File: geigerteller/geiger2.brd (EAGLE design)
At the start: 100 x 60 mm, 56 parts, among them J1 AVR_SPI_PRG_6PTH, Q1 NFET, Q2 MMBT5088, Q4 MMBT5088, Q5 MMBT5088, U1 ATMEGA328P, U2 MAX1555, U3 LCD-16X2SILK, U4 FT232RL-BASICSSOP, U5 MC34063SMD

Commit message: Moved drill holes and Q5
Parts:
- moved Q5 6.56 mm to (5.75, 53.2), turned to 270 degrees
- moved R1 5.06 mm to (2.50, 50.2)
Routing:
- net N$5: track 149.1 -> 135.2 mm
- net RESET: track 92.7 -> 82.5 mm
- net N$2: track 48.9 -> 54.1 mm
- net N$24: track 12.7 -> 9.82 mm
- net 12V: track 129.4 -> 127.6 mm
- net N$4: track 3.37 -> 4.73 mm
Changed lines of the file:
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@@
 <wire x1="100" y1="60" x2="0" y2="60" width="0" layer="20"/>
 <wire x1="0" y1="60" x2="0" y2="0" width="0" layer="20"/>
-<hole x="5.65" y="54.45" drill="3.2"/>
-<hole x="94.5" y="54.5" drill="3.2"/>
-<hole x="5.5" y="5.5" drill="3.2"/>
-<wire x1="0.25" y1="38.25" x2="99.5" y2="38.25" width="1.016" layer="51" style="longdash"/>
-<hole x="95.25" y="3.5" drill="3.2"/>
+<hole x="3" y="57" drill="3.2"/>
+<hole x="97" y="57" drill="3.2"/>
+<hole x="3" y="3" drill="3.2"/>
+<wire x1="0.25" y1="38.25" x2="99.5" y2="38.25" width="1.016" layer="121" style="longdash"/>
+<hole x="97" y="3" drill="3.2"/>
 </plain>
 <attributes>
@@
 <attribute name="NAME" x="74.891" y="54.202" size="0.4064" layer="25"/>
 </element>
-<element name="R1" library="rcl" package="R0603" value="330" x="7.25" y="48.5" smashed="yes" rot="R90">
-<attribute name="NAME" x="5.615" y="47.115" size="1.27" layer="25" rot="R90"/>
+<element name="R1" library="rcl" package="R0603" value="330" x="2.5" y="50.25" smashed="yes" rot="R90">
+<attribute name="NAME" x="4.615" y="49.615" size="1.27" layer="25" rot="R90"/>
 </element>
 <element name="R2" library="rcl" package="0207/10" value="" x="54.5" y="55.25" smashed="yes">
@@
 </element>
 <element name="U$2" library="henriks_egne_pakker" package="SOT23" value="XC6026" x="79.75" y="7.25" rot="R270"/>
-<element name="Q5" library="SparkFun-DiscreteSemi" package="SOT23" value="MMBT5088" x="10.75" y="49">
-<attribute name="PROD_ID" value="TRANS-11160" x="10.75" y="49" size="1.778" layer="27" display="off"/>
+<element name="Q5" library="SparkFun-DiscreteSemi" package="SOT23" value="MMBT5088" x="5.75" y="53.25" smashed="yes" rot="R270">
+<attribute name="PROD_ID" value="TRANS-11160" x="5.75" y="53.25" size="1.778" layer="27" rot="R270" display="off"/>
+<attribute name="NAME" x="5.611" y="50.532" size="1.016" layer="25"/>
 </element>
 <element name="R14" library="rcl" package="R0603" value="10k" x="8.7" y="56.7" smashed="yes" rot="R270">
@@
 <wire x1="35.25" y1="38.5" x2="33.25" y2="40.5" width="0.3048" layer="1"/>
 <wire x1="33.25" y1="40.5" x2="31.75" y2="40.5" width="0.3048" layer="1"/>
-<wire x1="7.25" y1="47.65" x2="7.25" y2="46.25" width="0.4064" layer="1"/>
 <via x="7.25" y="46.25" extent="1-16" drill="0.6" shape="octagon"/>
 <wire x1="7.25" y1="46.25" x2="7.25" y2="43.5" width="0.4064" layer="16"/>
 <wire x1="7.25" y1="43.5" x2="7.5" y2="43.25" width="0.4064" layer="16"/>
 <wire x1="7.5" y1="43.25" x2="10.75" y2="43.25" width="0.4064" layer="16"/>
+<wire x1="7.25" y1="46.25" x2="7.25" y2="47.25" width="0.4064" layer="1"/>
+<wire x1="7.25" y1="47.25" x2="5.5" y2="49" width="0.4064" layer="1"/>
+<wire x1="5.5" y1="49" x2="2.9" y2="49" width="0.4064" layer="1"/>
+<wire x1="2.9" y1="49" x2="2.5" y2="49.4" width="0.4064" layer="1"/>
 </signal>
 <signal name="N$3">
@@
 <wire x1="93.5" y1="37.5" x2="93.5" y2="29.5" width="0.3048" layer="16"/>
 <wire x1="93.5" y1="29.5" x2="95.25" y2="27.75" width="0.3048" layer="16"/>
-<wire x1="98.5" y1="6" x2="98.5" y2="1.5" width="0.3048" layer="1"/>
-<wire x1="91.5" y1="1.75" x2="91.5" y2="5.46" width="0.3048" layer="1"/>
-<wire x1="91.5" y1="5.46" x2="92.21" y2="5.46" width="0.3048" layer="1"/>
-<wire x1="92.21" y1="5.46" x2="93" y2="6.25" width="0.3048" layer="1"/>
-<wire x1="93" y1="6.25" x2="93" y2="7.46" width="0.3048" layer="1"/>
-<wire x1="93" y1="7.46" x2="93.54" y2="8" width="0.3048" layer="1"/>
 <wire x1="99" y1="6.5" x2="99" y2="9" width="0.3048" layer="16"/>
 <wire x1="99" y1="9" x2="98.5" y2="9.5" width="0.3048" layer="16"/>
@@
 <wire x1="95.5" y1="13" x2="95.25" y2="13.25" width="0.3048" layer="16"/>
 <wire x1="95.25" y1="13.25" x2="95.25" y2="27.75" width="0.3048" layer="16"/>
-<wire x1="98.5" y1="1.5" x2="97.75" y2="0.75" width="0.3048" layer="1"/>
-<wire x1="97.75" y1="0.75" x2="92.5" y2="0.75" width="0.3048" layer="1"/>
-<wire x1="92.5" y1="0.75" x2="91.5" y2="1.75" width="0.3048" layer="1"/>
+<wire x1="98.5" y1="6" x2="95.54" y2="6" width="0.3048" layer="1"/>
+<wire x1="95.54" y1="6" x2="93.54" y2="8" width="0.3048" layer="1"/>
 </signal>
 <signal name="N$6">
@@
 <via x="87.25" y="5.5" extent="1-16" drill="0.6" shape="octagon"/>
 <wire x1="87.25" y1="5.5" x2="90.25" y2="5.5" width="0.3048" layer="16"/>
-<wire x1="98.25" y1="4.75" x2="97.75" y2="5.25" width="0.3048" layer="16"/>
-<wire x1="97.75" y1="5.25" x2="97.75" y2="5.5" width="0.3048" layer="16"/>
-<wire x1="97.75" y1="5.5" x2="97.25" y2="6" width="0.3048" layer="16"/>
 <wire x1="97.25" y1="6" x2="97.25" y2="7.5" width="0.3048" layer="16"/>
 <wire x1="97.25" y1="7.5" x2="96.58" y2="7.5" width="0.3048" layer="16"/>
@@
 <wire x1="85.75" y1="5.75" x2="86" y2="5.5" width="0.3048" layer="16"/>
 <wire x1="86" y1="5.5" x2="87.25" y2="5.5" width="0.3048" layer="16"/>
-<wire x1="90.25" y1="5.5" x2="90.25" y2="2.25" width="0.3048" layer="16"/>
-<wire x1="90.25" y1="2.25" x2="91.75" y2="0.75" width="0.3048" layer="16"/>
-<wire x1="91.75" y1="0.75" x2="98" y2="0.75" width="0.3048" layer="16"/>
-<wire x1="98" y1="0.75" x2="98.25" y2="1" width="0.3048" layer="16"/>
-<wire x1="98.25" y1="1" x2="98.25" y2="4.75" width="0.3048" layer="16"/>
+<wire x1="97.25" y1="6" x2="97" y2="5.75" width="0.3048" layer="16"/>
+<wire x1="97" y1="5.75" x2="90.5" y2="5.75" width="0.3048" layer="16"/>
+<wire x1="90.5" y1="5.75" x2="90.25" y2="5.5" width="0.3048" layer="16"/>
 </signal>
 <signal name="LCD_E">
@@
 <wire x1="15" y1="52.25" x2="13.75" y2="51" width="0.3048" layer="1"/>
 <via x="13.75" y="51" extent="1-16" drill="0.6" shape="octagon"/>
-<wire x1="13.75" y1="51" x2="7.5" y2="51" width="0.3048" layer="16"/>
-<via x="7.5" y="51" extent="1-16" drill="0.6" shape="octagon"/>
-<wire x1="7.5" y1="51" x2="7.5" y2="53" width="0.3048" layer="1"/>
-<wire x1="7.5" y1="53" x2="8.75" y2="54.25" width="0.3048" layer="1"/>
-<wire x1="8.75" y1="54.25" x2="8.75" y2="55.8" width="0.3048" layer="1"/>
+<wire x1="13.75" y1="51" x2="8.75" y2="51" width="0.3048" layer="16"/>
+<via x="8.75" y="51" extent="1-16" drill="0.6" shape="octagon"/>
 <wire x1="8.75" y1="55.8" x2="8.7" y2="55.85" width="0.3048" layer="1"/>
 <via x="34" y="47.5" extent="1-16" drill="0.6" shape="octagon"/>
@@
 <wire x1="31.5" y1="57.25" x2="31.5" y2="55.1681" width="0.3048" layer="1"/>
 <wire x1="31.5" y1="55.1681" x2="31.4919" y2="55.16" width="0.3048" layer="1"/>
+<wire x1="8.75" y1="55.8" x2="8.75" y2="51" width="0.4064" layer="1"/>
 </signal>
 <signal name="N$4">
 <contactref element="R1" pad="2"/>
 <contactref element="Q5" pad="1"/>
-<wire x1="9.8" y1="47.9" x2="9.8" y2="48.2" width="0.4064" layer="1"/>
-<wire x1="9.8" y1="48.2" x2="8.6" y2="49.4" width="0.4064" layer="1"/>
-<wire x1="8.6" y1="49.4" x2="7.3" y2="49.4" width="0.4064" layer="1"/>
-<wire x1="7.3" y1="49.4" x2="7.25" y2="49.35" width="0.4064" layer="1"/>
+<wire x1="2.5" y1="51.1" x2="2.5" y2="53.25" width="0.4064" layer="1"/>
+<wire x1="2.5" y1="53.25" x2="3.5" y2="54.25" width="0.4064" layer="1"/>
+<wire x1="3.5" y1="54.25" x2="4.6" y2="54.25" width="0.4064" layer="1"/>
+<wire x1="4.6" y1="54.25" x2="4.65" y2="54.2" width="0.4064" layer="1"/>
 </signal>
 <signal name="N$24">
@@
 <contactref element="R14" pad="1"/>
 <contactref element="Q1" pad="1"/>
-<wire x1="10.75" y1="50.1" x2="10.75" y2="50.25" width="0.4064" layer="1"/>
-<wire x1="10.75" y1="50.25" x2="9" y2="52" width="0.4064" layer="1"/>
-<wire x1="9" y1="52" x2="9" y2="53.5" width="0.4064" layer="1"/>
-<wire x1="9" y1="53.5" x2="10" y2="54.5" width="0.4064" layer="1"/>
-<wire x1="10" y1="54.5" x2="10" y2="57.25" width="0.4064" layer="1"/>
 <wire x1="10" y1="57.25" x2="10.25" y2="57.5" width="0.4064" layer="1"/>
 <wire x1="10.25" y1="57.5" x2="10.75" y2="57.5" width="0.4064" layer="1"/>
@@
 <wire x1="8.7" y1="57.55" x2="10.7" y2="57.55" width="0.4064" layer="1"/>
 <wire x1="10.7" y1="57.55" x2="10.75" y2="57.5" width="0.4064" layer="1"/>
+<wire x1="6.85" y1="53.25" x2="6.85" y2="56.35" width="0.4064" layer="1"/>
+<wire x1="6.85" y1="56.35" x2="8" y2="57.5" width="0.4064" layer="1"/>
+<wire x1="8" y1="57.5" x2="8.65" y2="57.5" width="0.4064" layer="1"/>
+<wire x1="8.65" y1="57.5" x2="8.7" y2="57.55" width="0.4064" layer="1"/>
 </signal>
 <signal name="N$37">

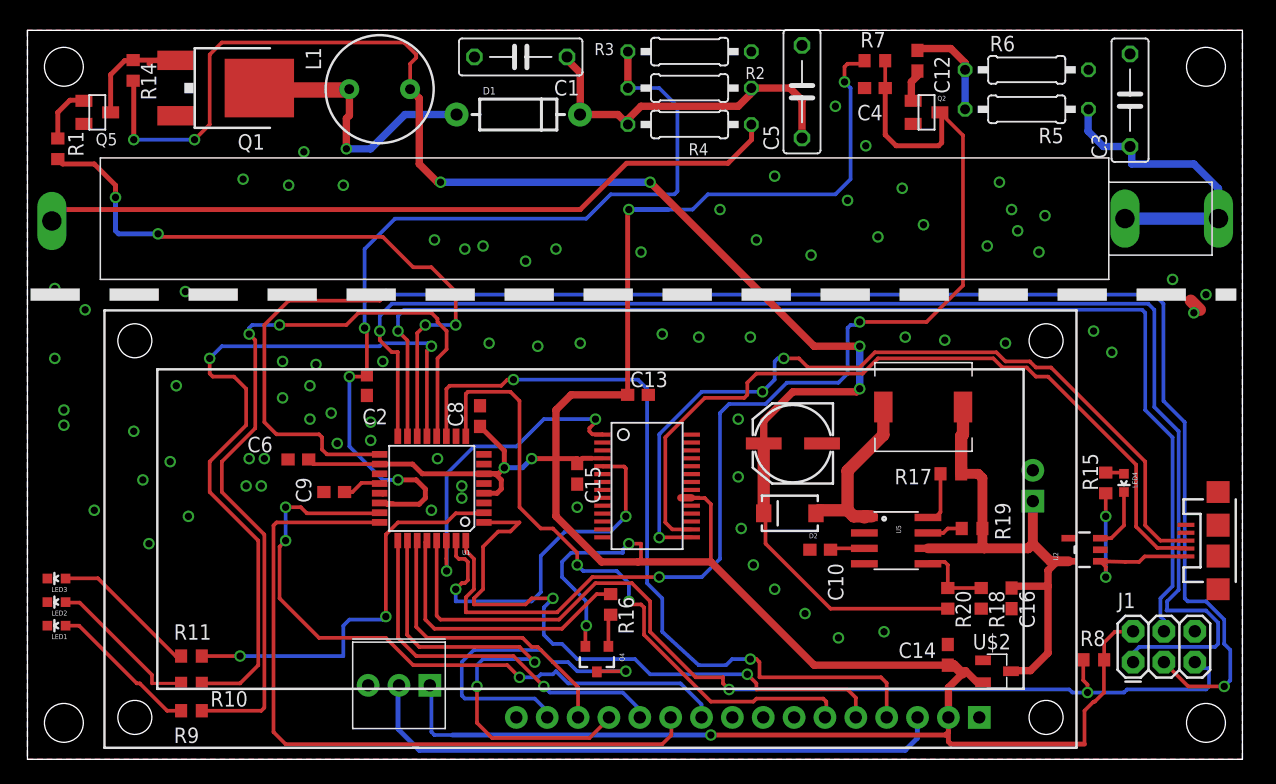
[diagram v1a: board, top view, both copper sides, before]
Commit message: Added C7, moved battery connector
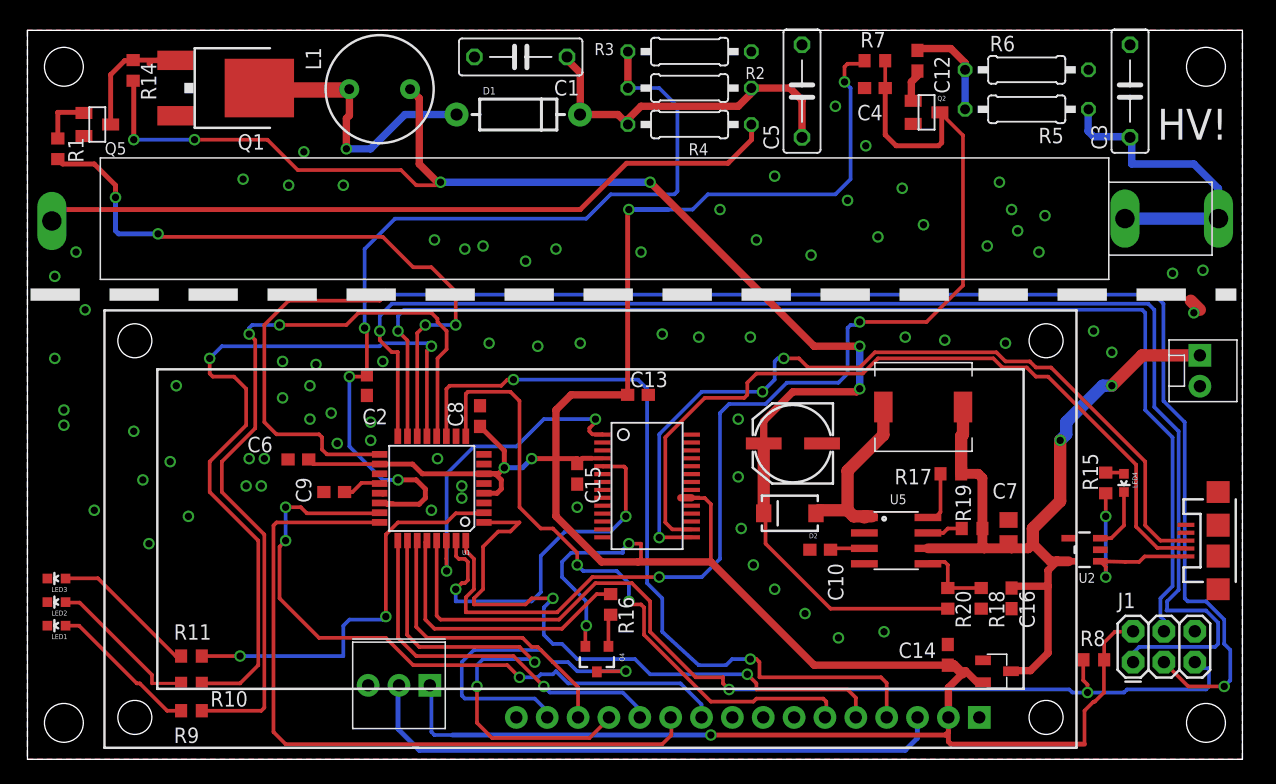
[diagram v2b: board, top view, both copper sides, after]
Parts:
- added C7: (no value), rcl:C0805
- moved LIPO 18.2 mm to (96.5, 33.2), flipped to the top, turned to 270 degrees
- moved Q5 1.00 mm to (5.75, 52.2)
- moved C3 0.75 mm to (90.8, 55.0)
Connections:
- net 6V: now also C7.1
- net GND: now also C7.2
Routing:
- net 6V: track 44.0 -> 65.4 mm, vias 0 -> 2
- net 12V: track 127.6 -> 121.1 mm
- net N$24: track 9.82 -> 10.8 mm
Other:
- board text added: "HV!"
